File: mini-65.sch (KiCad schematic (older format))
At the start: 173 parts, among them J1 AVR-ISP-6, SW1 SW_Push, U1 ATmega32U4-AU, Y1 Crystal_GND24_Small

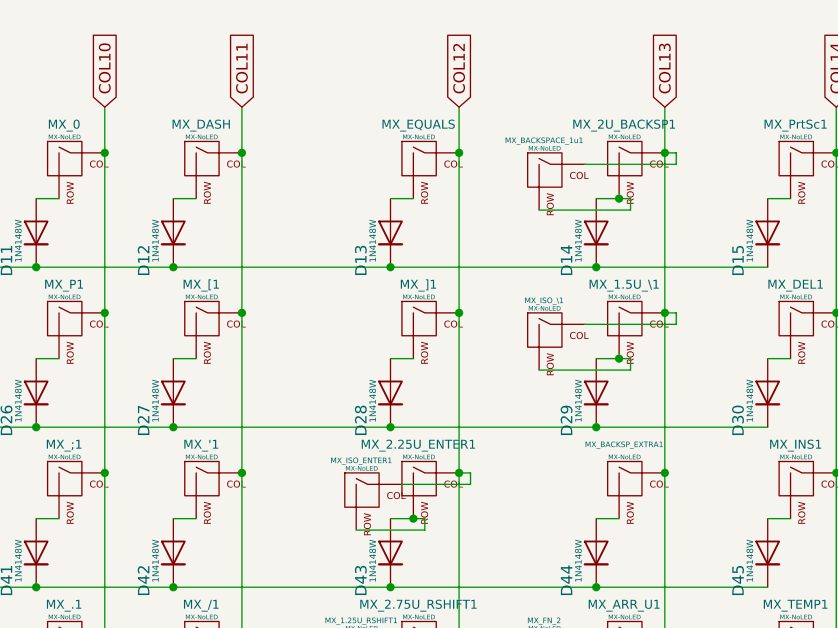
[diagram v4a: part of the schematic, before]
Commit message: Switched around ISO enter and ISO backslash
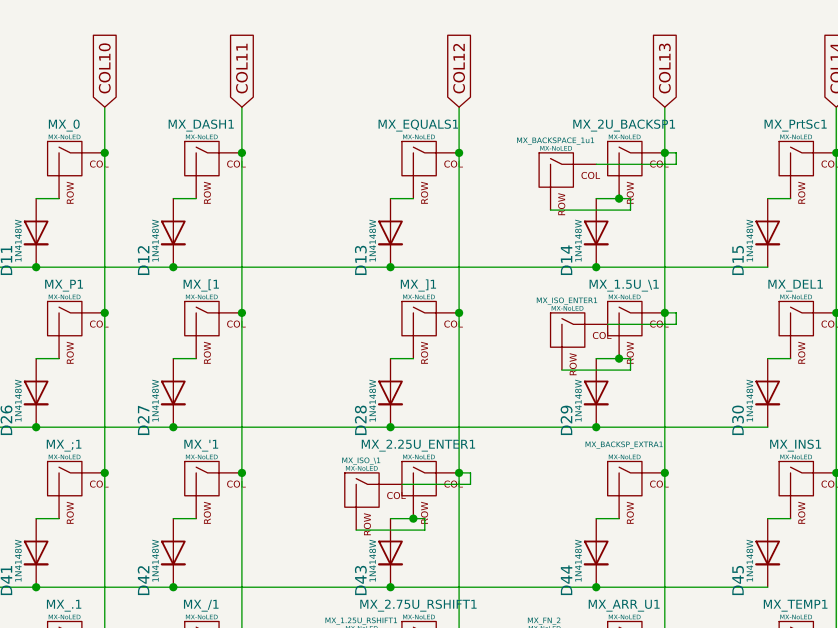
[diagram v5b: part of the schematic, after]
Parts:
- renumbered MX_DASH to MX_DASH1, MX_EQUALS to MX_EQUALS1
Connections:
- net COL12: now also MX_ISO_\1.1 (COL); no longer MX_ISO_ENTER1.1 (COL)
- net COL13: now also MX_ISO_ENTER1.1 (COL); no longer MX_ISO_\1.1 (COL)
- net at D43.2 (A), MX_2.25U_ENTER1.2 (ROW): now also MX_ISO_\1.2 (ROW); no longer MX_ISO_ENTER1.2 (ROW)
- net at D29.2 (A), MX_1.5U_\1.2 (ROW): now also MX_ISO_ENTER1.2 (ROW); no longer MX_ISO_\1.2 (ROW)
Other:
- moved on the sheet: MX_BACKSPACE_1u1, MX_ISO_ENTER1, MX_ISO_\1
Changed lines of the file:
@@
 	12250 1300 12150 1300
 $Comp
-L MX_Alps_Hybrid:MX-NoLED MX_EQUALS
+L MX_Alps_Hybrid:MX-NoLED MX_EQUALS1
 U 1 1 5F474929
 P 12300 1150
-F 0 "MX_EQUALS" H 12272 1324 39  0000 C CNN
+F 0 "MX_EQUALS1" H 12272 1324 39  0000 C CNN
 F 1 "MX-NoLED" H 12274 1269 20  0000 C CNN
 F 2 "MX_Alps_Hybrid:MX-1U-NoLED" H 11675 1125 60  0001 C CNN
@@
 L MX_Alps_Hybrid:MX-NoLED MX_BACKSPACE_1u1
 U 1 1 612DBC93
-P 12850 1200
-F 0 "MX_BACKSPACE_1u1" H 12822 1354 24  0000 C CNN
-F 1 "MX-NoLED" H 12824 1319 20  0000 C CNN
-F 2 "MX_Alps_Hybrid:MX-1U-NoLED" H 12225 1175 60  0001 C CNN
-F 3 "" H 12225 1175 60  0001 C CNN
-	1    12850 1200
+P 12900 1200
+F 0 "MX_BACKSPACE_1u1" H 12872 1354 24  0000 C CNN
+F 1 "MX-NoLED" H 12874 1319 20  0000 C CNN
+F 2 "MX_Alps_Hybrid:MX-1U-NoLED" H 12275 1175 60  0001 C CNN
+F 3 "" H 12275 1175 60  0001 C CNN
+	1    12900 1200
 	1    0    0    -1
 $EndComp
@@
 	13400 1100 13400 1150
 Wire Wire Line
-	13400 1150 13000 1150
+	13400 1150 13050 1150
 Connection ~ 13150 1300
 $Comp
 L MX_Alps_Hybrid:MX-NoLED MX_ISO_ENTER1
 U 1 1 61322262
+P 12950 1900
+F 0 "MX_ISO_ENTER1" H 12922 2054 24  0000 C CNN
+F 1 "MX-NoLED" H 12924 2019 20  0000 C CNN
+F 2 "MX_Only:MXOnly-ISO-ROTATED-ReversedStabilizers-NoLED" H 12325 1875 60  0001 C CNN
+F 3 "" H 12325 1875 60  0001 C CNN
+	1    12950 1900
+	1    0    0    -1
+$EndComp
+Wire Wire Line
+	12450 2500 12500 2500
+Wire Wire Line
+	12500 2500 12500 2550
+Wire Wire Line
+	12500 2550 12200 2550
+Connection ~ 12250 2700
+$Comp
+L MX_Alps_Hybrid:MX-NoLED MX_ISO_\1
+U 1 1 61369504
 P 12050 2600
-F 0 "MX_ISO_ENTER1" H 12022 2754 24  0000 C CNN
+F 0 "MX_ISO_\\1" H 12022 2754 24  0000 C CNN
 F 1 "MX-NoLED" H 12024 2719 20  0000 C CNN
-F 2 "MX_Only:MXOnly-ISO-ROTATED-ReversedStabilizers-NoLED" H 11425 2575 60  0001 C CNN
+F 2 "MX_Alps_Hybrid:MX-1U-NoLED" H 11425 2575 60  0001 C CNN
 F 3 "" H 11425 2575 60  0001 C CNN
 	1    12050 2600
@@
 $EndComp
 Wire Wire Line
-	12450 2500 12500 2500
-Wire Wire Line
-	12500 2500 12500 2550
-Wire Wire Line
-	12500 2550 12200 2550
-Connection ~ 12250 2700
-$Comp
-L MX_Alps_Hybrid:MX-NoLED MX_ISO_\1
-U 1 1 61369504
-P 12850 1900
-F 0 "MX_ISO_\\1" H 12822 2054 24  0000 C CNN
-F 1 "MX-NoLED" H 12824 2019 20  0000 C CNN
-F 2 "MX_Alps_Hybrid:MX-1U-NoLED" H 12225 1875 60  0001 C CNN
-F 3 "" H 12225 1875 60  0001 C CNN
-	1    12850 1900
-	1    0    0    -1
-$EndComp
-Wire Wire Line
 	13350 1800 13400 1800
 Wire Wire Line
 	13400 1800 13400 1850
 Wire Wire Line
-	13400 1850 13000 1850
+	13400 1850 13100 1850
 Connection ~ 13150 2000
 $Comp
@@
 	13200 1300 13200 1350
 Wire Wire Line
-	12800 1350 13200 1350
+	12850 1350 13200 1350
 Wire Wire Line
 	13150 2000 13200 2000
@@
 	13200 2000 13200 2050
 Wire Wire Line
-	12800 2050 13200 2050
+	12900 2050 13200 2050
 Wire Wire Line
 	10700 4100 10750 4100
@@
 $EndComp
 $Comp
-L MX_Alps_Hybrid:MX-NoLED MX_DASH
+L MX_Alps_Hybrid:MX-NoLED MX_DASH1
 U 1 1 5F45D4DD
 P 11350 1150
-F 0 "MX_DASH" H 11322 1324 39  0000 C CNN
+F 0 "MX_DASH1" H 11322 1324 39  0000 C CNN
 F 1 "MX-NoLED" H 11324 1269 20  0000 C CNN
 F 2 "MX_Alps_Hybrid:MX-1U-NoLED" H 10725 1125 60  0001 C CNN

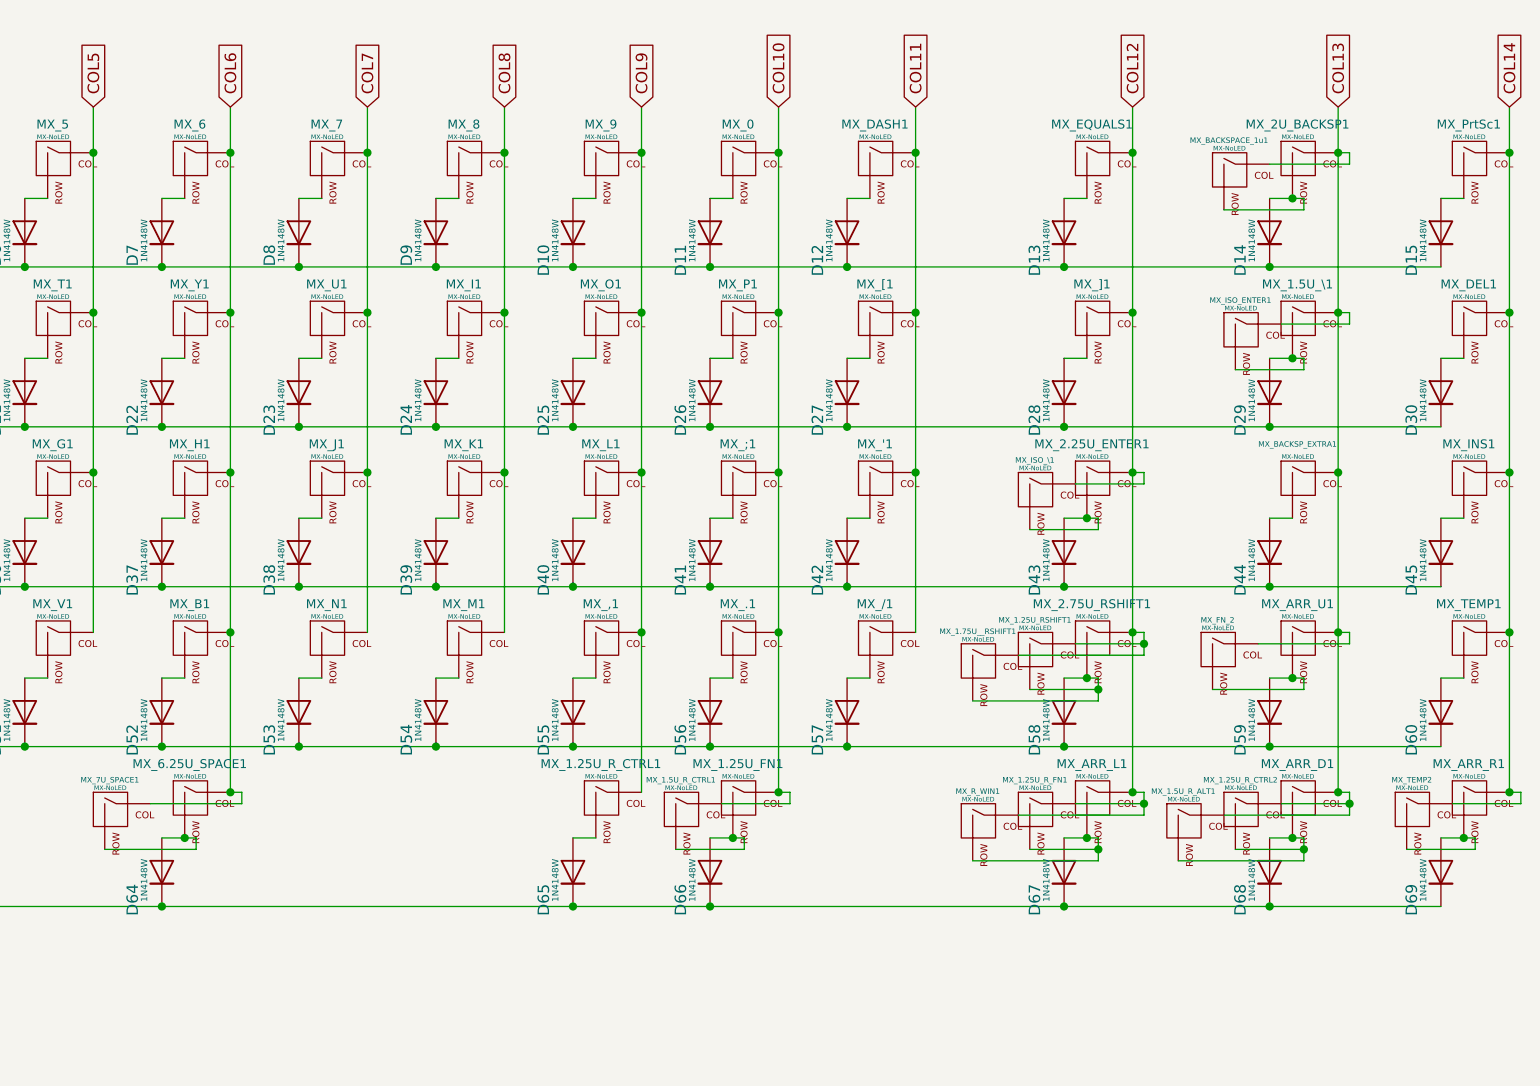
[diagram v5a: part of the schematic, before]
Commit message: Moved around some of the diode locations
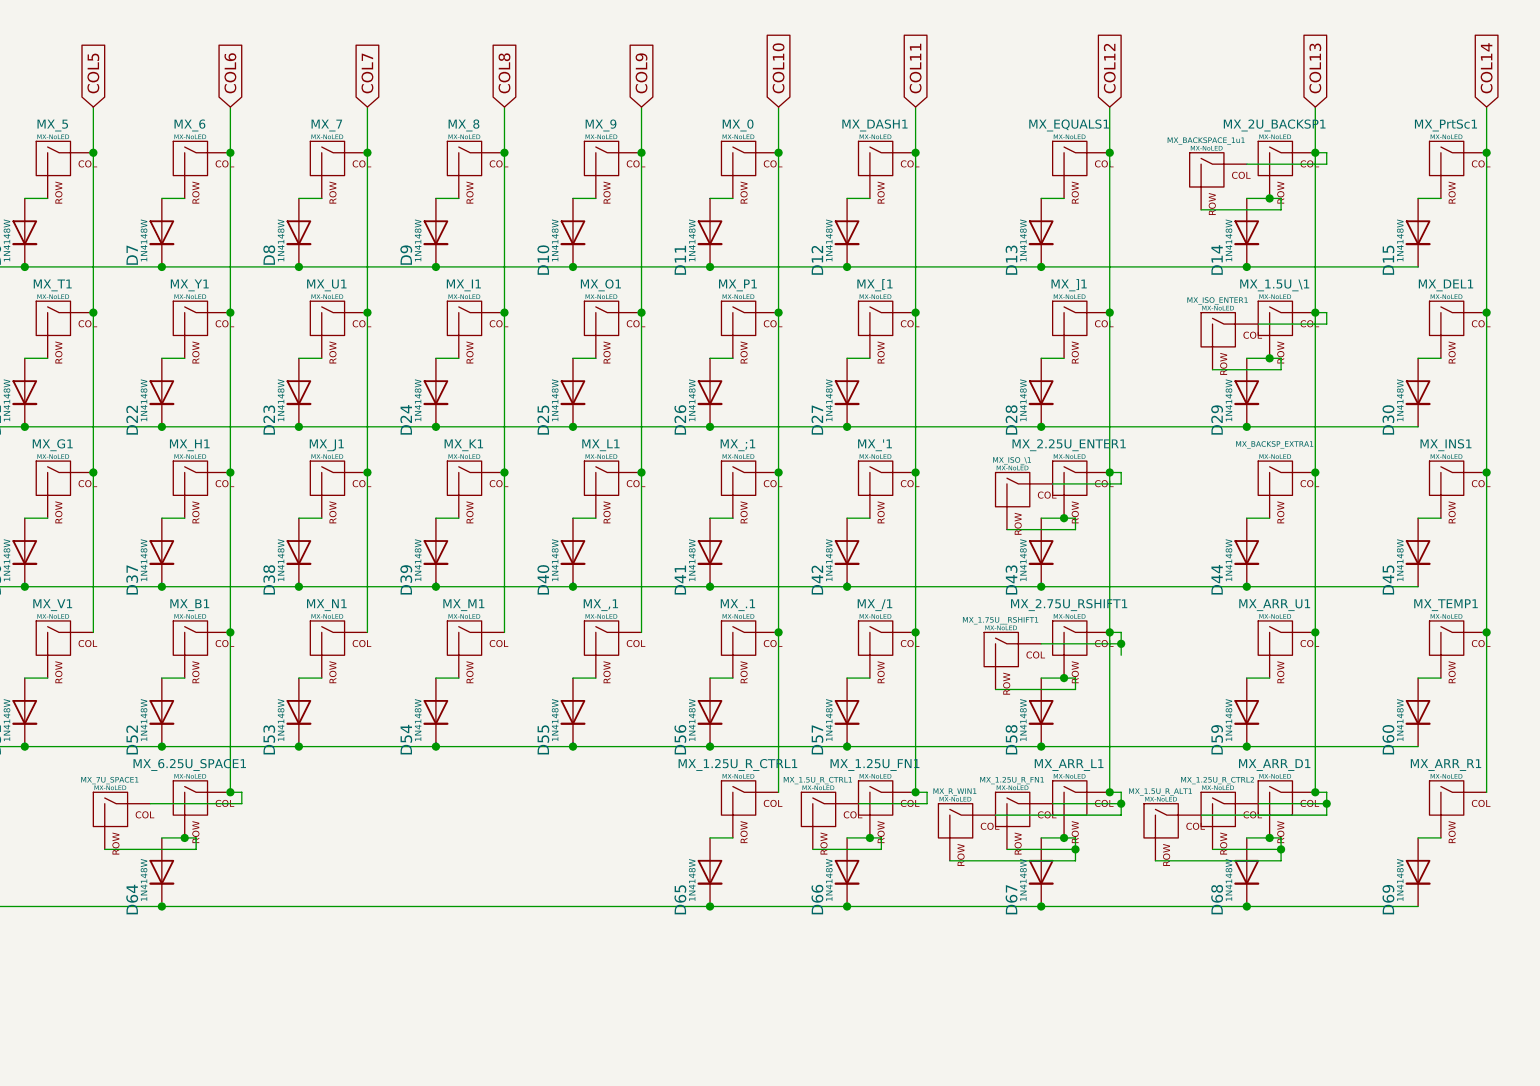
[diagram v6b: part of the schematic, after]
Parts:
- removed MX_1.25U_RSHIFT1: MX-NoLED, MX_Alps_Hybrid:MX-1.25U-NoLED, symbol MX_Alps_Hybrid:MX-NoLED
- removed MX_FN_2, MX_TEMP2: MX-NoLED, MX_Alps_Hybrid:MX-1U-NoLED, symbol MX_Alps_Hybrid:MX-NoLED
- MX_'1, MX_,1, MX_.1, MX_/1, MX_0, MX_1, MX_2, MX_3, MX_4, MX_5, MX_6, MX_7, MX_8, MX_9, MX_;1, MX_A1, MX_ARR_D1, MX_ARR_L1, MX_ARR_R1, MX_ARR_U1, MX_B1, MX_BACKSPACE_1u1, MX_BACKSP_EXTRA1, MX_C1, MX_D1, MX_DASH1, MX_DEL1, MX_E1, MX_EQUALS1, MX_ESC1, MX_F1, MX_G1, MX_H1, MX_I1, MX_INS1, MX_ISO_\1, MX_J1, MX_K1, MX_L1, MX_L_BSLASH1, MX_L_WIN1, MX_M1, MX_N1, MX_O1, MX_P1, MX_PrtSc1, MX_Q1, MX_R1, MX_R_WIN1, MX_S1, MX_STEP_CAPS1, MX_T1, MX_TEMP1, MX_U1, MX_V1, MX_W1, MX_X1, MX_Y1, MX_Z1, MX_[1, MX_]1: footprint MX_Alps_Hybrid:MX-1U-NoLED -> MX_Only:MXOnly-1U-NoLED
- MX_1.25U_FN1, MX_1.25U_L_ALT1, MX_1.25U_L_CTRL1, MX_1.25U_L_SHIFT1, MX_1.25U_L_WIN1, MX_1.25U_R_CTRL1, MX_1.25U_R_CTRL2, MX_1.25U_R_FN1: footprint MX_Alps_Hybrid:MX-1.25U-NoLED -> MX_Only:MXOnly-1.25U-NoLED
- MX_1.5U_L_ALT1, MX_1.5U_L_CTRL1, MX_1.5U_R_ALT1, MX_1.5U_R_CTRL1, MX_1.5U_TAB1, MX_1.5U_\1: footprint MX_Alps_Hybrid:MX-1.5U-NoLED -> MX_Only:MXOnly-1.5U-NoLED
- MX_1.75U_CAPSLOCK1, MX_1.75U__RSHIFT1: footprint MX_Alps_Hybrid:MX-1.75U-NoLED -> MX_Only:MXOnly-1.75U-NoLED
- MX_2.25U_ENTER1, MX_2.25U_LSHIFT1: footprint MX_Alps_Hybrid:MX-2.25U-NoLED -> MX_Only:MXOnly-2.25U-NoLED
- MX_2.75U_RSHIFT1: footprint MX_Alps_Hybrid:MX-2.75U-NoLED -> MX_Only:MXOnly-2.75U-NoLED
- MX_2U_BACKSP1: footprint MX_Alps_Hybrid:MX-2U-NoLED -> MX_Only:MXOnly-2U-NoLED
- MX_6.25U_SPACE1: footprint MX_Alps_Hybrid:MX-6.25U-NoLED -> MX_Only:MXOnly-6.25U-NoLED
- MX_7U_SPACE1: footprint MX_Alps_Hybrid:MX-7U-NoLED -> MX_Only:MXOnly-7U-NoLED
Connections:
- net COL10: now also MX_1.25U_R_CTRL1.1 (COL); no longer MX_1.25U_FN1.1 (COL), MX_1.5U_R_CTRL1.1 (COL)
- net COL11: now also MX_1.25U_FN1.1 (COL), MX_1.5U_R_CTRL1.1 (COL)
- net COL9: no longer MX_1.25U_R_CTRL1.1 (COL)
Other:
- moved on the sheet: D13, D14, D15, D28, D29, D30, D43, D44, D45, D58, D59, D60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

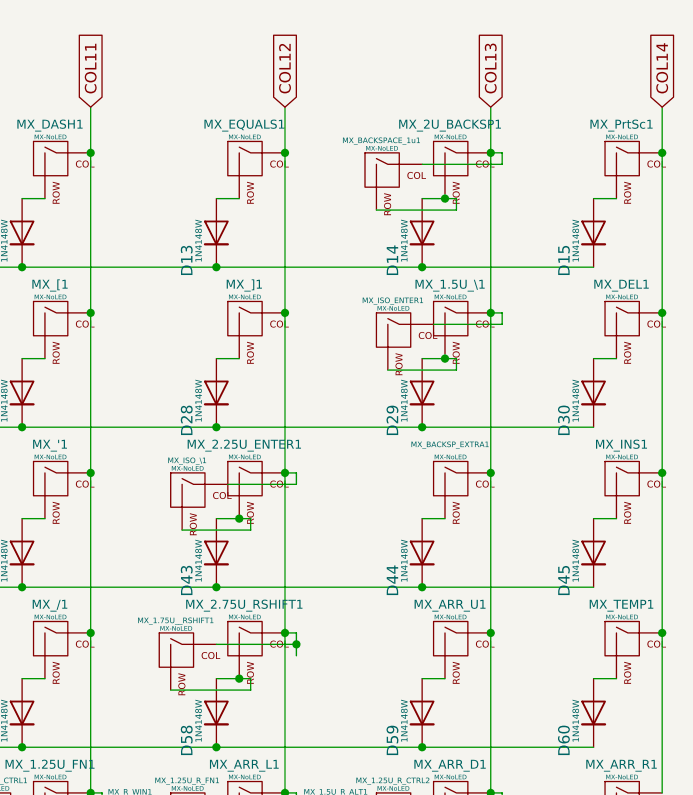
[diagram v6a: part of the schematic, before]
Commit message: Moved the diodes down a bit
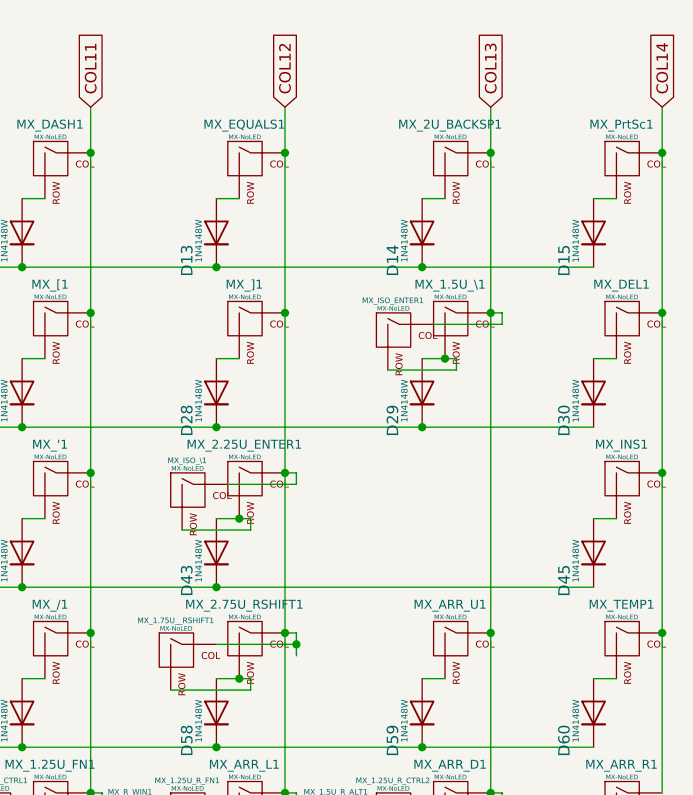
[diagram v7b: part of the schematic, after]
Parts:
- removed D44: 1N4148W, canadian_footprints:D_SOD123_axial-dual, symbol Diode:1N4148W
- removed MX_BACKSPACE_1u1, MX_BACKSP_EXTRA1: MX-NoLED, MX_Only:MXOnly-1U-NoLED, symbol MX_Alps_Hybrid:MX-NoLED
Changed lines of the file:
@@
 	0    -1   -1   0
 $EndComp
-Wire Wire Line
-	13050 2700 12950 2700
-$Comp
-L MX_Alps_Hybrid:MX-NoLED MX_BACKSP_EXTRA1
-U 1 1 61221643
-P 13100 2550
-F 0 "MX_BACKSP_EXTRA1" H 13072 2724 24  0000 C CNN
-F 1 "MX-NoLED" H 13074 2669 20  0000 C CNN
-F 2 "MX_Only:MXOnly-1U-NoLED" H 12475 2525 60  0001 C CNN
-F 3 "" H 12475 2525 60  0001 C CNN
-	1    13100 2550
-	1    0    0    -1
-$EndComp
-$Comp
-L Diode:1N4148W D44
-U 1 1 61221649
-P 12950 2850
-F 0 "D44" H 12899 2978 50  0000 R CNN
-F 1 "1N4148W" H 13009 2927 28  0000 R CNN
-F 2 "canadian_footprints:D_SOD123_axial-dual" H 12950 2675 50  0001 C CNN
-F 3 "https://www.vishay.com/docs/85748/1n4148w.pdf" H 12950 2850 50  0001 C CNN
-	1    12950 2850
-	0    -1   -1   0
-$EndComp
-Wire Wire Line
-	13250 1800 13250 2500
 Connection ~ 13250 1800
-Connection ~ 13250 2500
-$Comp
-L MX_Alps_Hybrid:MX-NoLED MX_BACKSPACE_1u1
-U 1 1 612DBC93
-P 12800 1200
-F 0 "MX_BACKSPACE_1u1" H 12772 1354 24  0000 C CNN
-F 1 "MX-NoLED" H 12774 1319 20  0000 C CNN
-F 2 "MX_Only:MXOnly-1U-NoLED" H 12175 1175 60  0001 C CNN
-F 3 "" H 12175 1175 60  0001 C CNN
-	1    12800 1200
-	1    0    0    -1
-$EndComp
-Wire Wire Line
-	13250 1100 13300 1100
-Wire Wire Line
-	13300 1100 13300 1150
-Wire Wire Line
-	13300 1150 12950 1150
-Connection ~ 13050 1300
 $Comp
 L MX_Alps_Hybrid:MX-NoLED MX_ISO_ENTER1
@@
 	12050 2300 12950 2300
 Wire Wire Line
-	12050 3000 12950 3000
-Wire Wire Line
 	12050 4400 12950 4400
 Wire Wire Line
@@
 	13100 4150 13100 4200
 Connection ~ 13250 3200
-Wire Wire Line
-	13250 3200 13250 2500
 Wire Wire Line
 	13250 3200 13250 3900
@@
 	11900 2750 12200 2750
 Wire Wire Line
-	13050 1300 13100 1300
-Wire Wire Line
-	13100 1300 13100 1350
-Wire Wire Line
-	12750 1350 13100 1350
-Wire Wire Line
 	13050 2000 13100 2000
 Wire Wire Line
@@
 	12950 3700 13700 3700
 Connection ~ 12950 3700
-Wire Wire Line
-	12950 3000 13700 3000
-Connection ~ 12950 3000
 Wire Wire Line
 	12950 2300 13700 2300
@@
 Connection ~ 11200 4400
 Connection ~ 12050 4400
+Wire Wire Line
+	13250 1800 13250 3200
+Wire Wire Line
+	12050 3000 13700 3000
 $EndSCHEMATC
